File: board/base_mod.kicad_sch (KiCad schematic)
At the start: 33 parts, among them J3 RS-232, J4 LCD, Q5 BC548, Q6 BC548, SW10 MENU, SW3 RI, SW4 UP, SW5 LE, SW6 OK, SW7 DN, SW8 CANCEL, SW9 BACK, U4 AT24C1024B, U5 MAX3232, U6 24LCxxx, U7 MCP23008-xP, U8 BOB-12009

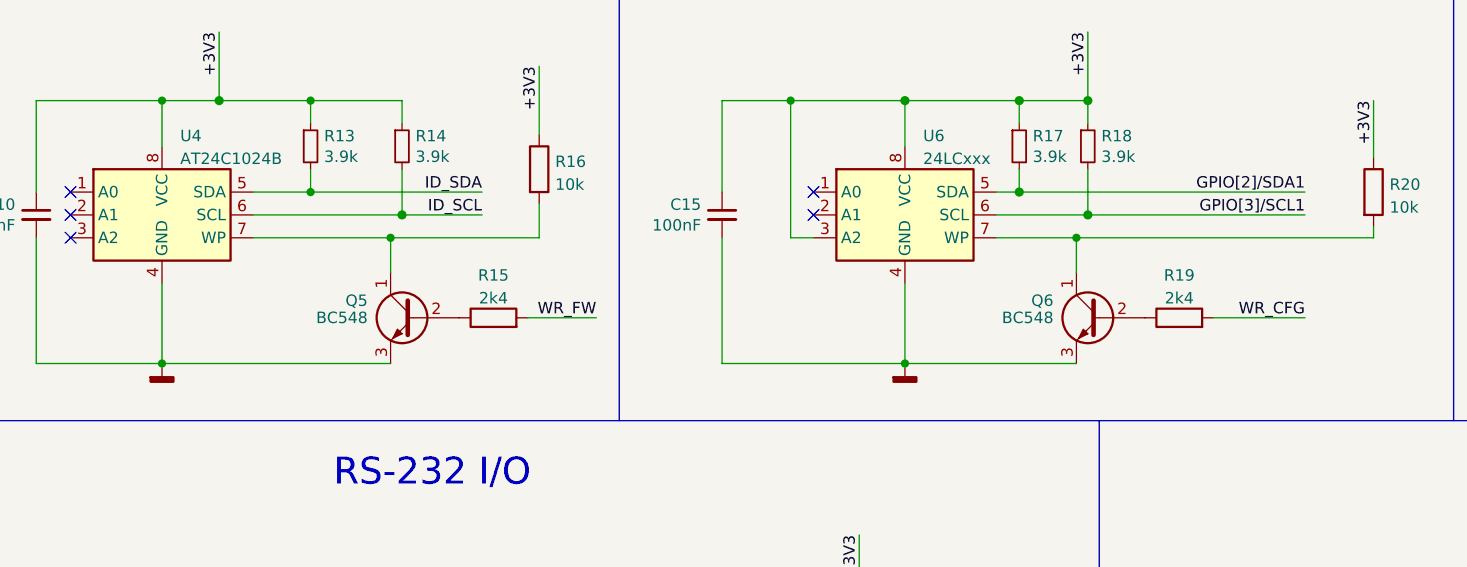
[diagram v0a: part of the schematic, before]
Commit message: Fix typos and label names.
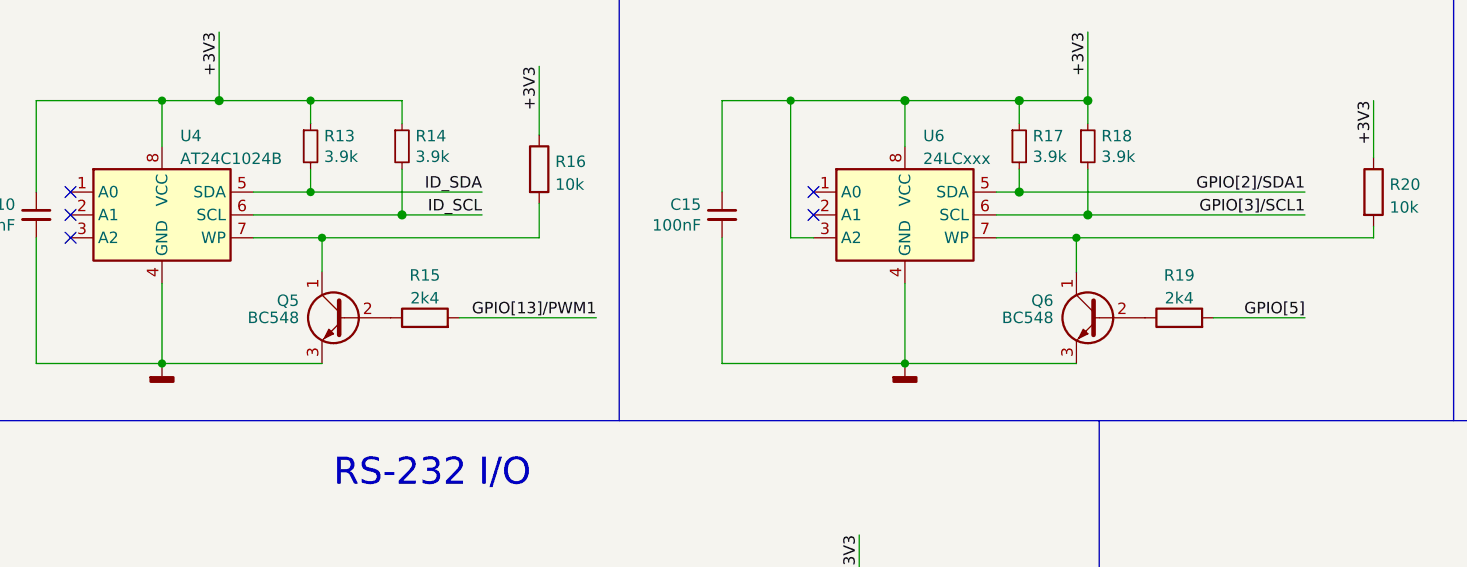
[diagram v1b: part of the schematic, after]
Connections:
- net WR_CFG renamed GPIO[5]
- net WR_FW renamed GPIO[13]/PWM1
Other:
- moved on the sheet: Q5, R15
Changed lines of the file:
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@@
   (junction (at 69.85 88.9) (diameter 0) (color 0 0 0 0)
   )
-  (junction (at 63.5 48.26) (diameter 0) (color 0 0 0 0)
+  (junction (at 55.88 48.26) (diameter 0) (color 0 0 0 0)
   )
   (junction (at 199.39 93.98) (diameter 0) (color 0 0 0 0)
@@
     (stroke (width 0) (type default) (color 0 0 0 0))
   )
-  (wire (pts (xy 63.5 48.26) (xy 63.5 52.07))
+  (wire (pts (xy 55.88 48.26) (xy 55.88 52.07))
     (stroke (width 0) (type default) (color 0 0 0 0))
   )
@@
     (stroke (width 0) (type default) (color 0 0 0 0))
   )
+  (wire (pts (xy 55.88 48.26) (xy 80.01 48.26))
+    (stroke (width 0) (type default) (color 0 0 0 0))
+  )
   (wire (pts (xy 175.26 93.98) (xy 177.8 93.98))
     (stroke (width 0) (type default) (color 0 0 0 0))
@@
     (stroke (width 0) (type default) (color 0 0 0 0))
   )
-  (wire (pts (xy 38.1 62.23) (xy 63.5 62.23))
+  (wire (pts (xy 38.1 62.23) (xy 55.88 62.23))
     (stroke (width 0) (type default) (color 0 0 0 0))
   )
@@
     (stroke (width 0) (type default) (color 0 0 0 0))
   )
-  (wire (pts (xy 48.26 48.26) (xy 63.5 48.26))
-    (stroke (width 0) (type default) (color 0 0 0 0))
-  )
-  (wire (pts (xy 80.01 44.45) (xy 80.01 48.26))
+  (wire (pts (xy 48.26 48.26) (xy 55.88 48.26))
     (stroke (width 0) (type default) (color 0 0 0 0))
   )
@@
     (stroke (width 0) (type default) (color 0 0 0 0))
   )
-  (wire (pts (xy 63.5 48.26) (xy 80.01 48.26))
-    (stroke (width 0) (type default) (color 0 0 0 0))
-  )
   (wire (pts (xy 99.06 146.05) (xy 99.06 153.67))
     (stroke (width 0) (type default) (color 0 0 0 0))
@@
     (stroke (width 0) (type default) (color 0 0 0 0))
   )
+  (wire (pts (xy 80.01 48.26) (xy 80.01 44.45))
+    (stroke (width 0) (type default) (color 0 0 0 0))
+  )
   (wire (pts (xy 99.06 153.67) (xy 69.85 153.67))
     (stroke (width 0) (type default) (color 0 0 0 0))
@@
     (stroke (width 0) (type solid) (color 0 0 0 0))
   )
-  (wire (pts (xy 78.74 57.15) (xy 86.36 57.15))
+  (wire (pts (xy 71.12 57.15) (xy 86.36 57.15))
     (stroke (width 0) (type default) (color 0 0 0 0))
   )
@@
     (effects (font (size 3 3)) (justify left bottom))
   )
+  (label "GPIO[13]{slash}PWM1" (at 86.36 57.15 180)
+    (effects (font (size 1.27 1.27)) (justify right bottom))
+  )
   (label "GPIO[2]{slash}SDA1" (at 185.42 41.91 0)
     (effects (font (size 1.27 1.27)) (justify left bottom))
@@
     (effects (font (size 1.27 1.27)) (justify right bottom))
   )
+  (label "GPIO[5]" (at 165.1 57.15 180)
+    (effects (font (size 1.27 1.27)) (justify right bottom))
+  )
   (label "GPIO[3]{slash}SCL1" (at 146.05 109.22 0)
     (effects (font (size 1.27 1.27)) (justify left bottom))
@@
     (effects (font (size 1.27 1.27)) (justify right bottom))
   )
-  (label "WR_CFG" (at 165.1 57.15 180)
-    (effects (font (size 1.27 1.27)) (justify right bottom))
-  )
   (label "+3V3" (at 80.01 29.21 270)
     (effects (font (size 1.27 1.27)) (justify right bottom))
@@
   (label "GPIO[19]{slash}PCM.FS" (at 146.05 116.84 0)
     (effects (font (size 1.27 1.27)) (justify left bottom))
-  )
-  (label "WR_FW" (at 86.36 57.15 180)
-    (effects (font (size 1.27 1.27)) (justify right bottom))
   )
   (label "GPIO[15]{slash}RXD0" (at 30.48 135.89 0)
@@
     (pin "2")
   )
-  (symbol (lib_id "Transistor_BJT:BC548") (at 66.04 57.15 0) (mirror y) (unit 1)
+  (symbol (lib_id "Transistor_BJT:BC548") (at 58.42 57.15 0) (mirror y) (unit 1)
     (in_bom yes) (on_board yes)
-    (property "Reference" "Q5" (id 0) (at 60.96 55.245 0)
+    (property "Reference" "Q5" (id 0) (at 53.34 55.245 0)
       (effects (font (size 1.27 1.27)) (justify left))
     )
-    (property "Value" "BC548" (id 1) (at 60.96 57.15 0)
+    (property "Value" "BC548" (id 1) (at 53.34 57.15 0)
       (effects (font (size 1.27 1.27)) (justify left))
     )
-    (property "Footprint" "Package_TO_SOT_THT:TO-92_Inline" (id 2) (at 60.96 59.055 0)
+    (property "Footprint" "Package_TO_SOT_THT:TO-92_Inline" (id 2) (at 53.34 59.055 0)
       (effects (font (size 1.27 1.27) italic) (justify left) hide)
     )
-    (property "Datasheet" "https://www.onsemi.com/pub/Collateral/BC550-D.pdf" (id 3) (at 66.04 57.15 0)
+    (property "Datasheet" "https://www.onsemi.com/pub/Collateral/BC550-D.pdf" (id 3) (at 58.42 57.15 0)
       (effects (font (size 1.27 1.27)) (justify left) hide)
     )
@@
     (pin "2")
   )
-  (symbol (lib_id "Device:R") (at 74.93 57.15 90) (unit 1)
+  (symbol (lib_id "Device:R") (at 67.31 57.15 90) (unit 1)
     (in_bom yes) (on_board yes) (fields_autoplaced)
-    (property "Reference" "R15" (id 0) (at 74.93 52.4342 90))
-    (property "Value" "2k4" (id 1) (at 74.93 54.9711 90))
-    (property "Footprint" "" (id 2) (at 74.93 58.928 90)
+    (property "Reference" "R15" (id 0) (at 67.31 52.4342 90))
+    (property "Value" "2k4" (id 1) (at 67.31 54.9711 90))
+    (property "Footprint" "" (id 2) (at 67.31 58.928 90)
       (effects (font (size 1.27 1.27)) hide)
     )
-    (property "Datasheet" "~" (id 3) (at 74.93 57.15 0)
+    (property "Datasheet" "~" (id 3) (at 67.31 57.15 0)
       (effects (font (size 1.27 1.27)) hide)
     )

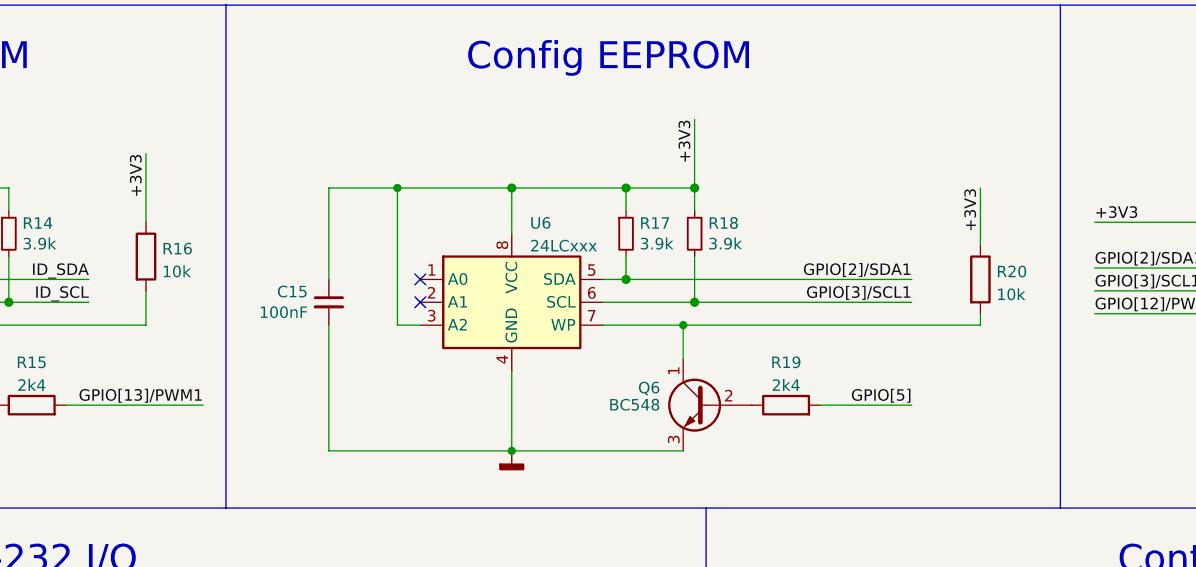
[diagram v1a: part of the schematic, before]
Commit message: Change EEPROM write protection Ppull-up resistor value to 1k.
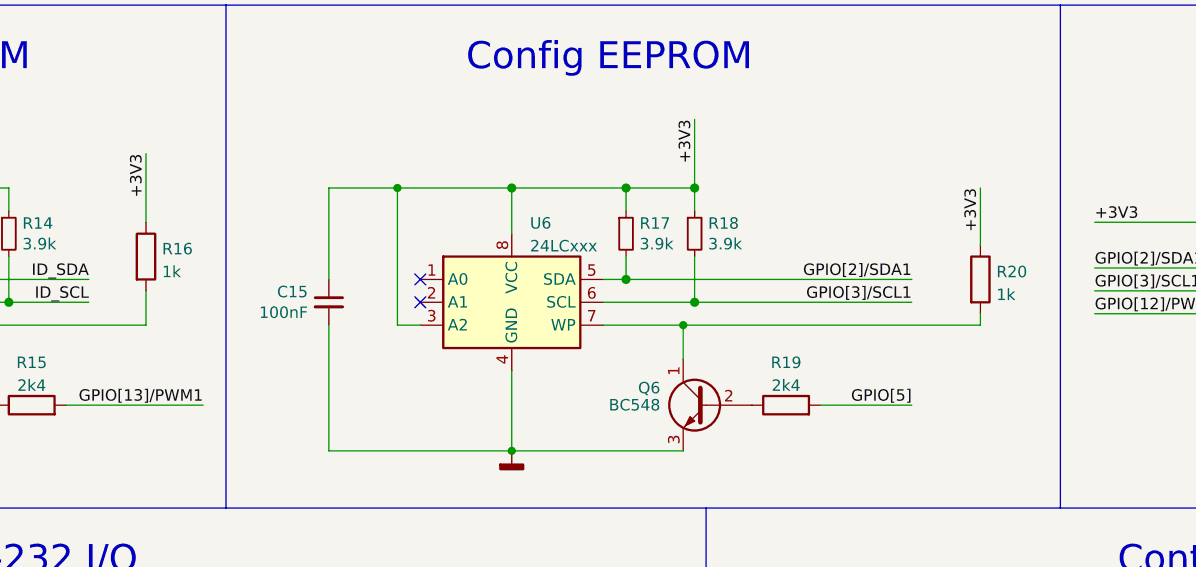
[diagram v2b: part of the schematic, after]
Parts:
- R16, R20: value 10k -> 1k
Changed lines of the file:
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@@
       (effects (font (size 1.27 1.27)) (justify left))
     )
-    (property "Value" "10k" (id 1) (at 174.498 44.8822 0)
+    (property "Value" "1k" (id 1) (at 174.498 44.8822 0)
       (effects (font (size 1.27 1.27)) (justify left))
     )
@@
       (effects (font (size 1.27 1.27)) (justify left))
     )
-    (property "Value" "10k" (id 1) (at 81.788 42.3422 0)
+    (property "Value" "1k" (id 1) (at 81.788 42.3422 0)
       (effects (font (size 1.27 1.27)) (justify left))
     )

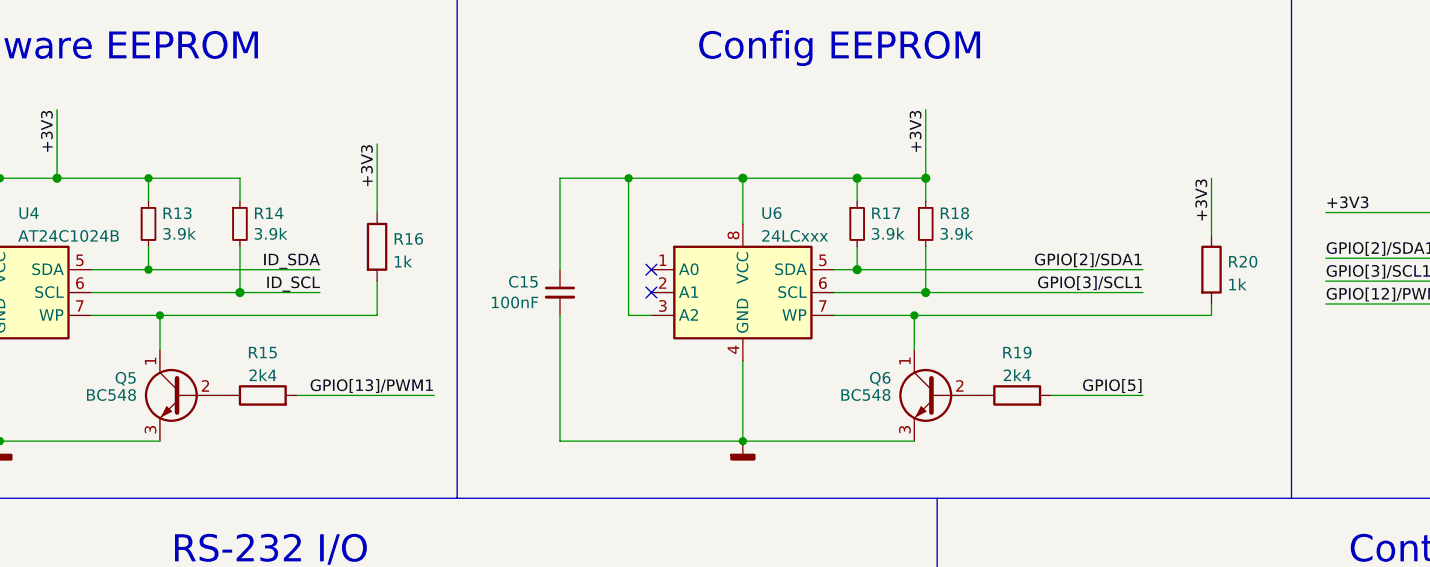
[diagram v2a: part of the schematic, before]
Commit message: Improve power circuit and protection.
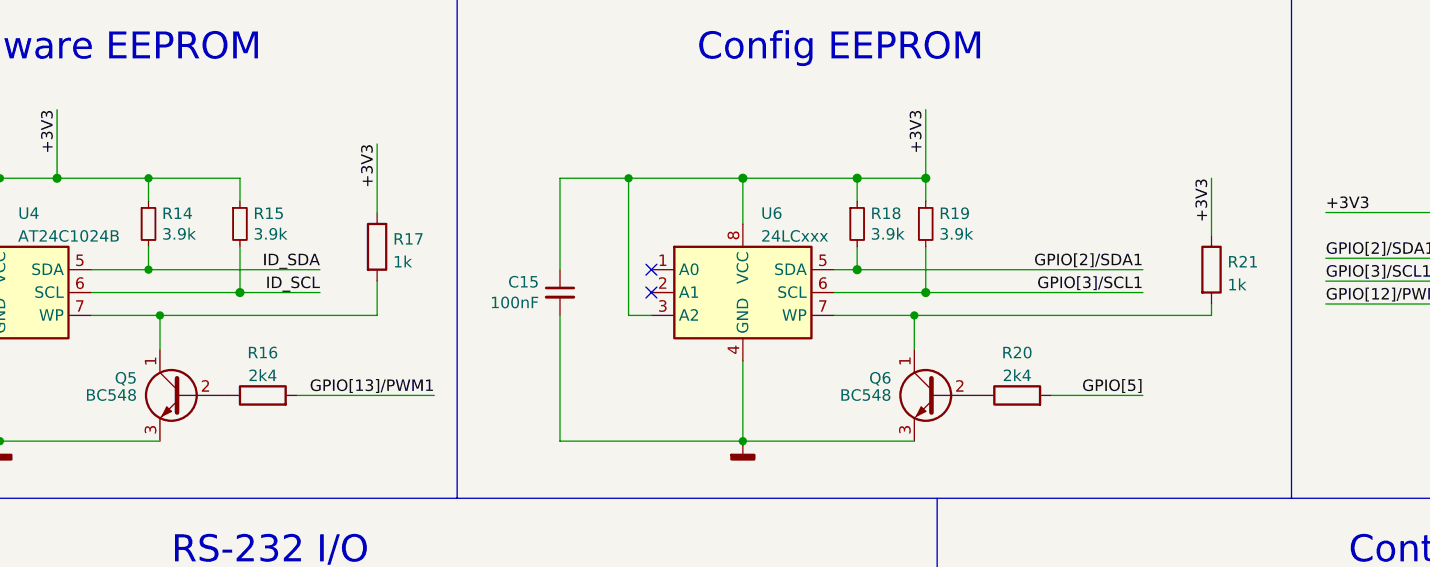
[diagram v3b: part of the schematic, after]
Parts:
- renumbered R13 to R14, R14 to R15, R15 to R16, R16 to R17, R17 to R18, R18 to R19, R19 to R20, R20 to R21
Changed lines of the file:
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@@
   (symbol (lib_id "Device:R") (at 67.31 57.15 90) (unit 1)
     (in_bom yes) (on_board yes) (fields_autoplaced)
-    (property "Reference" "R15" (id 0) (at 67.31 52.4342 90))
+    (property "Reference" "R16" (id 0) (at 67.31 52.4342 90))
     (property "Value" "2k4" (id 1) (at 67.31 54.9711 90))
     (property "Footprint" "" (id 2) (at 67.31 58.928 90)
@@
   (symbol (lib_id "Device:R") (at 172.72 43.18 0) (unit 1)
     (in_bom yes) (on_board yes) (fields_autoplaced)
-    (property "Reference" "R20" (id 0) (at 174.498 42.3453 0)
+    (property "Reference" "R21" (id 0) (at 174.498 42.3453 0)
       (effects (font (size 1.27 1.27)) (justify left))
     )
@@
   (symbol (lib_id "Device:R_Small") (at 133.35 38.1 0) (unit 1)
     (in_bom yes) (on_board yes)
-    (property "Reference" "R17" (id 0) (at 134.8486 36.957 0)
+    (property "Reference" "R18" (id 0) (at 134.8486 36.957 0)
       (effects (font (size 1.27 1.27)) (justify left))
     )
@@
   (symbol (lib_id "Device:R") (at 80.01 40.64 0) (unit 1)
     (in_bom yes) (on_board yes) (fields_autoplaced)
-    (property "Reference" "R16" (id 0) (at 81.788 39.8053 0)
+    (property "Reference" "R17" (id 0) (at 81.788 39.8053 0)
       (effects (font (size 1.27 1.27)) (justify left))
     )
@@
   (symbol (lib_id "Device:R_Small") (at 140.97 38.1 0) (unit 1)
     (in_bom yes) (on_board yes)
-    (property "Reference" "R18" (id 0) (at 142.4686 36.957 0)
+    (property "Reference" "R19" (id 0) (at 142.4686 36.957 0)
       (effects (font (size 1.27 1.27)) (justify left))
     )
@@
   (symbol (lib_id "Device:R") (at 151.13 57.15 90) (unit 1)
     (in_bom yes) (on_board yes) (fields_autoplaced)
-    (property "Reference" "R19" (id 0) (at 151.13 52.4342 90))
+    (property "Reference" "R20" (id 0) (at 151.13 52.4342 90))
     (property "Value" "2k4" (id 1) (at 151.13 54.9711 90))
     (property "Footprint" "" (id 2) (at 151.13 58.928 90)
@@
   (symbol (lib_id "Device:R_Small") (at 54.61 38.1 0) (unit 1)
     (in_bom yes) (on_board yes)
-    (property "Reference" "R13" (id 0) (at 56.1086 36.957 0)
+    (property "Reference" "R14" (id 0) (at 56.1086 36.957 0)
       (effects (font (size 1.27 1.27)) (justify left))
     )
@@
   (symbol (lib_id "Device:R_Small") (at 64.77 38.1 0) (unit 1)
     (in_bom yes) (on_board yes)
-    (property "Reference" "R14" (id 0) (at 66.2686 36.957 0)
-      (effects (font (size 1.27 1.27)) (justify left))
-    )
+    (property "Reference" "R15" (id 0) (at 66.2686 36.957 0)
+      (effects (font (size 1.27 1.27)) (justify left))
+    )

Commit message: Do some cleanup after recent changes.
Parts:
- J3: footprint (none) -> Connector_Dsub:DSUB-9_Male_Horizontal_P2.77x2.84mm_EdgePinOffset9.40mm
- J4: footprint (none) -> Connector_PinHeader_2.54mm:PinHeader_1x05_P2.54mm_Vertical_SMD_Pin1Right
- U8: footprint CONV_BOB-12009 -> BOB-12009:CONV_BOB-12009
- renumbered C10 to C13, C11 to C14, C12 to C15, C13 to C16, C14 to C17, C15 to C18, C16 to C19, C17 to C20
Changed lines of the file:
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@@
   (title_block
     (title "The Ulysses Board")
-    (date "2022-09-04")
+    (date "2022-09-08")
     (rev "1.3")
     (company "Dirk Gottschalk")
@@
   (symbol (lib_id "Device:C_Small") (at 100.33 45.72 0) (unit 1)
     (in_bom yes) (on_board yes)
-    (property "Reference" "C15" (id 0) (at 98.0058 44.5706 0)
+    (property "Reference" "C18" (id 0) (at 98.0058 44.5706 0)
       (effects (font (size 1.27 1.27)) (justify right))
     )
@@
       (effects (font (size 1.27 1.27)) (justify left))
     )
-    (property "Footprint" "" (id 2) (at 110.49 135.89 0)
+    (property "Footprint" "Connector_Dsub:DSUB-9_Male_Horizontal_P2.77x2.84mm_EdgePinOffset9.40mm" (id 2) (at 110.49 135.89 0)
       (effects (font (size 1.27 1.27)) hide)
     )
@@
   (symbol (lib_id "Device:C_Polarized") (at 95.25 104.14 0) (unit 1)
     (in_bom yes) (on_board yes) (fields_autoplaced)
-    (property "Reference" "C14" (id 0) (at 98.171 102.4163 0)
+    (property "Reference" "C17" (id 0) (at 98.171 102.4163 0)
       (effects (font (size 1.27 1.27)) (justify left))
     )
@@
       (effects (font (size 1.27 1.27)) (justify right))
     )
-    (property "Footprint" "" (id 2) (at 248.92 44.45 0)
+    (property "Footprint" "Connector_PinHeader_2.54mm:PinHeader_1x05_P2.54mm_Vertical_SMD_Pin1Right" (id 2) (at 248.92 44.45 0)
       (effects (font (size 1.27 1.27)) hide)
     )
@@
   (symbol (lib_id "Device:C_Polarized") (at 41.91 104.14 0) (unit 1)
     (in_bom yes) (on_board yes) (fields_autoplaced)
-    (property "Reference" "C12" (id 0) (at 44.831 102.4163 0)
+    (property "Reference" "C15" (id 0) (at 44.831 102.4163 0)
       (effects (font (size 1.27 1.27)) (justify left))
     )
@@
   (symbol (lib_id "Device:C_Polarized") (at 111.76 113.03 90) (unit 1)
     (in_bom yes) (on_board yes)
-    (property "Reference" "C16" (id 0) (at 111.76 106.68 90))
+    (property "Reference" "C19" (id 0) (at 111.76 106.68 90))
     (property "Value" "1µF" (id 1) (at 111.76 109.22 90))
     (property "Footprint" "" (id 2) (at 115.57 112.0648 0)
@@
   (symbol (lib_id "Device:C_Polarized") (at 24.13 93.98 0) (unit 1)
     (in_bom yes) (on_board yes) (fields_autoplaced)
-    (property "Reference" "C11" (id 0) (at 27.051 92.2563 0)
+    (property "Reference" "C14" (id 0) (at 27.051 92.2563 0)
       (effects (font (size 1.27 1.27)) (justify left))
     )
@@
   (symbol (lib_id "Device:C_Small") (at 24.13 45.72 0) (unit 1)
     (in_bom yes) (on_board yes)
-    (property "Reference" "C10" (id 0) (at 21.8058 44.5706 0)
+    (property "Reference" "C13" (id 0) (at 21.8058 44.5706 0)
       (effects (font (size 1.27 1.27)) (justify right))
     )
@@
   (symbol (lib_id "Device:C_Polarized") (at 93.98 120.65 270) (mirror x) (unit 1)
     (in_bom yes) (on_board yes)
-    (property "Reference" "C13" (id 0) (at 93.98 114.3 90))
+    (property "Reference" "C16" (id 0) (at 93.98 114.3 90))
     (property "Value" "1µF" (id 1) (at 93.98 116.84 90))
     (property "Footprint" "" (id 2) (at 90.17 119.6848 0)
@@
   (symbol (lib_id "Device:C") (at 181.61 93.98 90) (unit 1)
     (in_bom yes) (on_board yes) (fields_autoplaced)
-    (property "Reference" "C17" (id 0) (at 181.61 88.1212 90))
+    (property "Reference" "C20" (id 0) (at 181.61 88.1212 90))
     (property "Value" "100nF" (id 1) (at 181.61 90.6581 90))
     (property "Footprint" "" (id 2) (at 185.42 93.0148 0)
@@
     (property "Reference" "U8" (id 0) (at 219.71 30.5902 0))
     (property "Value" "BOB-12009" (id 1) (at 219.71 33.1271 0))
-    (property "Footprint" "CONV_BOB-12009" (id 2) (at 219.71 44.45 0)
+    (property "Footprint" "BOB-12009:CONV_BOB-12009" (id 2) (at 219.71 44.45 0)
       (effects (font (size 1.27 1.27)) (justify left bottom) hide)
     )
